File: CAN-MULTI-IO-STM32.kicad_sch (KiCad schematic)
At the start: 63 parts, among them J1 H GND L, J2 TERM, J3 USART1, J5 PWR IN, U1 STM32L433RCT3, U2 MCP2562-E-SN, U3 LMR54410, U4 ADS1015IDGS, U5 PCA9537, U6 TCA9511

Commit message: fix 2.54mm terminal block issues
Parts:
- ANA_IN1: value Conn_01x06 -> 1725698
- GPIO1: renamed from GPIO_CON1; value Conn_01x06 -> 1725698
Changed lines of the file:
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@@
 		(dnp no)
 		(fields_autoplaced yes)
-		(property "Reference" "GPIO_CON1"
+		(property "Reference" "GPIO1"
 			(at 260.35 119.38 0)
 			(effects
@@
 			)
 		)
-		(property "Value" "Conn_01x06"
+		(property "Value" "1725698"
 			(at 260.35 121.92 0)
 			(effects
@@
 					(size 1.27 1.27)
 				)
+				(hide yes)
 			)
 		)
@@
 			)
 		)
-		(property "Datasheet" "~"
+		(property "Datasheet" "https://www.mouser.com/datasheet/3/507/9/phoenix_contact_1725698_en.pdf"
 			(at 260.35 133.35 0)
 			(effects
@@
 			)
 		)
-		(property "Description" "Generic connector, single row, 01x06, script generated (kicad-library-utils/schlib/autogen/connector/)"
+		(property "Description" "Phoenix Contact 1725698"
 			(at 260.35 133.35 0)
 			(effects
@@
 			(project "CAN-MULTI-IO-STM32"
 				(path "/807782eb-8307-4922-8e5a-50da44718f8e"
-					(reference "GPIO_CON1")
+					(reference "GPIO1")
 					(unit 1)
 				)
@@
 			)
 		)
-		(property "Value" "Conn_01x06"
+		(property "Value" "1725698"
 			(at 257.81 88.8999 0)
 			(effects
@@
 				)
 				(justify left)
+				(hide yes)
 			)
 		)
@@
 			)
 		)
-		(property "Datasheet" "~"
+		(property "Datasheet" "https://www.mouser.com/datasheet/3/507/9/phoenix_contact_1725698_en.pdf"
 			(at 260.35 86.36 0)
 			(effects
@@
 			)
 		)
-		(property "Description" "Generic connector, single row, 01x06, script generated (kicad-library-utils/schlib/autogen/connector/)"
+		(property "Description" "Phoenix Contact 1725698"
 			(at 260.35 86.36 0)
 			(effects

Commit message: fix a few footprint and drc issues
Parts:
- added CVDIV1: 100n, Capacitor_SMD:C_0603_1608Metric_Pad1.08x0.95mm_HandSolder, symbol Device:C_Small
- added RVDIV1: 4K7, Resistor_SMD:R_0603_1608Metric_Pad0.98x0.95mm_HandSolder, symbol Device:R_US
- added RVDIV2: 1K0, Resistor_SMD:R_0603_1608Metric_Pad0.98x0.95mm_HandSolder, symbol Device:R_US
- U6: value TCA9511 -> PI6ULS5V9511AUEX; footprint Package_SO:VSSOP-8_3x3mm_P0.65mm -> Package_SO:MSOP-8_3x3mm_P0.65mm; Height 1.1 -> (none); Manufacturer_Name Texas Instruments -> (none); Manufacturer_Part_Number TCA9511ADGKR -> (none); Mouser Part Number 595-TCA9511ADGKR -> (none); Mouser Price/Stock https://www.mouser.co.uk/ProductDetail/Texas-Instruments/TC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 -> (none)
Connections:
- net +12V: now also RVDIV1.1
- net GND: now also CVDIV1.2, RVDIV2.2
- net STATUS: now also U1.15 (PA1); no longer U1.16 (PA2)
- new net VDIV: CVDIV1.1, RVDIV1.2, RVDIV2.1, U1.16 (PA2)
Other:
- moved on the sheet: J5

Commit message: rename gpio header
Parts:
- renumbered ANA_IN1 to ANALOG_IN1, GPIO1 to DIGITAL_IO1
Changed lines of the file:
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@@
 		(dnp no)
 		(fields_autoplaced yes)
-		(property "Reference" "GPIO1"
+		(property "Reference" "DIGITAL_IO1"
 			(at 260.35 119.38 0)
 			(effects
@@
 			(project "CAN-MULTI-IO-STM32"
 				(path "/807782eb-8307-4922-8e5a-50da44718f8e"
-					(reference "GPIO1")
+					(reference "DIGITAL_IO1")
 					(unit 1)
 				)
@@
 		(on_board yes)
 		(dnp no)
-		(property "Reference" "ANA_IN1"
+		(property "Reference" "ANALOG_IN1"
 			(at 257.81 86.3599 0)
 			(effects
@@
 			(project ""
 				(path "/807782eb-8307-4922-8e5a-50da44718f8e"
-					(reference "ANA_IN1")
+					(reference "ANALOG_IN1")
 					(unit 1)
 				)

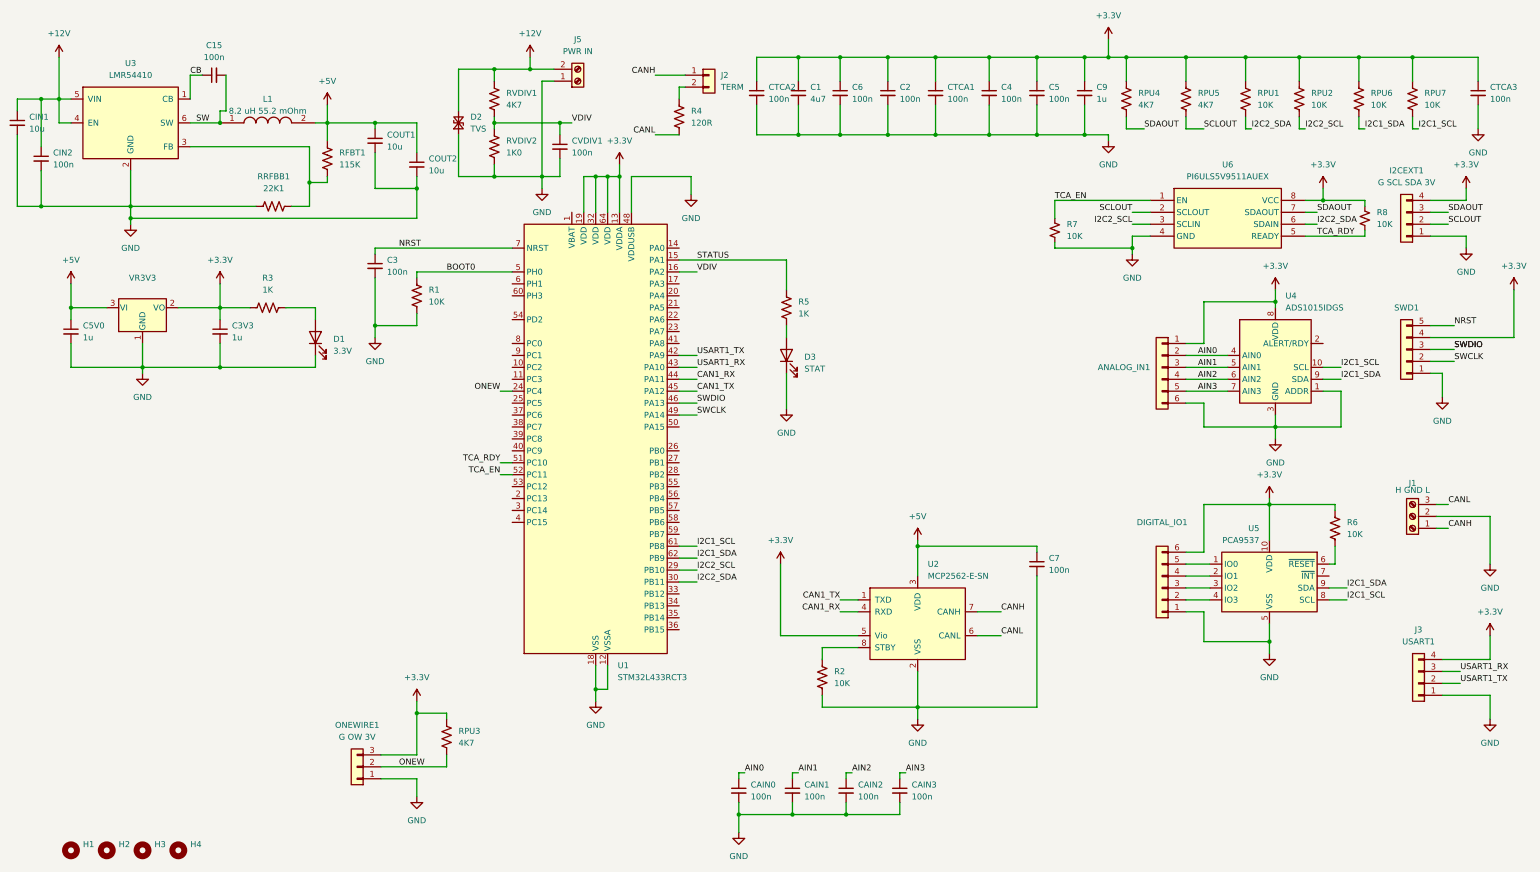
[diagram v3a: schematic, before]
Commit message: switch to STM32G0B1 micro, refactor pcb layout
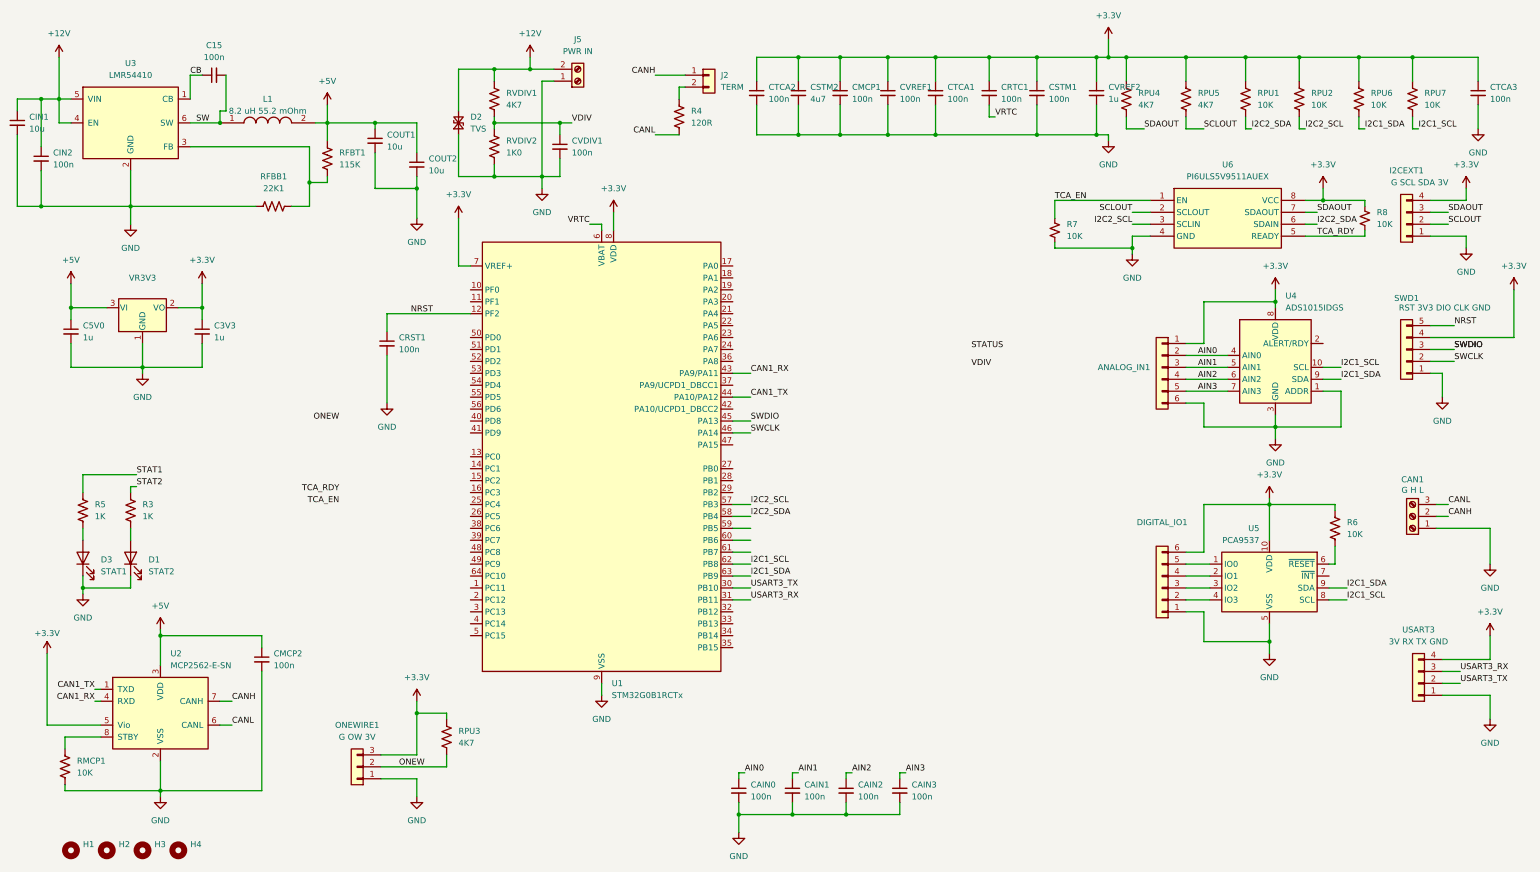
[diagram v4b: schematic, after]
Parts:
- removed R1: 10K, Resistor_SMD:R_0603_1608Metric_Pad0.98x0.95mm_HandSolder, symbol Device:R_US
- removed U1: STM32L433RCT3, Package_QFP:LQFP-64_10x10mm_P0.5mm, symbol MCU_ST_STM32L4:STM32L433RBTx
- added U1: STM32G0B1RCTx, Package_QFP:LQFP-64_10x10mm_P0.5mm, symbol MCU_ST_STM32G0:STM32G0B1RCTx
- CAN1: renamed from J1; value H GND L -> G H L; footprint TerminalBlock_Phoenix:TerminalBlock_Phoenix_MKDS-1,5-3_1x03_P5.00mm_Horizontal -> TerminalBlock_TE-Connectivity:TerminalBlock_TE_282834-3_1x03_P2.54mm_Horizontal
- D1: value 3.3V -> STAT2
- D3: value STAT -> STAT1
- SWD1: value STLINK -> RST 3V3 DIO CLK GND
- USART3: renamed from J3; value USART1 -> 3V RX TX GND
- renumbered C6 to CMCP1, C7 to CMCP2, C3 to CRST1, C4 to CRTC1, C5 to CSTM1, C1 to CSTM2, C2 to CVREF1, C9 to CVREF2, RRFBB1 to RFBB1, R2 to RMCP1
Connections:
- net +3.3V: now also U1.7 (VREF+), U1.8 (VDD); no longer R3.1
- net CAN1_RX: now also U1.43 (PA9/PA11)
- net CAN1_TX: now also U1.44 (PA10/PA12)
- net CANH: now also CAN1.2 (Pin_2); no longer CAN1.1 (Pin_1)
- net GND: now also CAN1.1 (Pin_1), U1.9 (VSS); no longer CAN1.2 (Pin_2), CRTC1.2
- net I2C1_SCL: now also U1.62 (PB8)
- net I2C1_SDA: now also U1.63 (PB9)
- net I2C2_SCL: now also U1.57 (PB3)
- net I2C2_SDA: now also U1.58 (PB4)
- net NRST: now also U1.12 (PF2)
- net STATUS: no longer R5.2
- net SWCLK: now also U1.46 (PA14)
- net SWDIO: now also U1.45 (PA13)
- net at D1.2 (A): now also R3.1; no longer R3.2
- net USART1_RX renamed USART3_RX
- net USART3_RX: now also U1.31 (PB11)
- net USART1_TX renamed USART3_TX
- net USART3_TX: now also U1.30 (PB10)
- new net STAT1: R5.2
- new net STAT2: R3.2
- new net VRTC: CRTC1.2, U1.6 (VBAT)
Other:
- moved on the sheet: C3V3, CMCP2, CRST1, CVREF2, D1, D3, R3, R5, RMCP1, U2

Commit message: final commit for tonight
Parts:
- CAN1: footprint TerminalBlock_TE-Connectivity:TerminalBlock_TE_282834-3_1x03_P2.54mm_Horizontal -> TerminalBlock_Phoenix:TerminalBlock_Phoenix_MPT-0,5-3-2.54_1x03_P2.54mm_Horizontal
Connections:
- net ONEW: now also U1.37 (PA9/UCPD1_DBCC1)
- net STAT1: now also U1.15 (PC2)
- net STAT2: now also U1.16 (PC3)
- net TCA_EN: now also U1.59 (PB5)
- net TCA_RDY: now also U1.56 (PD6)
- net VDIV: now also U1.17 (PA0)
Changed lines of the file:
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@@
+	(wire
+		(pts
+			(xy 110.49 95.25) (xy 113.03 95.25)
+		)
+		(stroke
+			(width 0)
+			(type default)
+		)
+	)
 	(wire
 		(pts
@@
 	(wire
 		(pts
+			(xy 168.91 64.77) (xy 172.72 64.77)
+		)
+		(stroke
+			(width 0)
+			(type default)
+		)
+	)
+	(wire
+		(pts
 			(xy 101.6 173.99) (xy 101.6 177.8)
 		)
@@
 	(wire
 		(pts
+			(xy 168.91 90.17) (xy 172.72 90.17)
+		)
+		(stroke
+			(width 0)
+			(type default)
+		)
+	)
+	(wire
+		(pts
 			(xy 40.64 52.07) (xy 21.59 52.07)
 		)
@@
 	(wire
 		(pts
+			(xy 110.49 113.03) (xy 113.03 113.03)
+		)
+		(stroke
+			(width 0)
+			(type default)
+		)
+	)
+	(wire
+		(pts
 			(xy 265.43 125.73) (xy 269.24 125.73)
 		)
@@
 		(pts
 			(xy 78.74 39.37) (xy 78.74 46.99)
+		)
+		(stroke
+			(width 0)
+			(type default)
+		)
+	)
+	(wire
+		(pts
+			(xy 110.49 110.49) (xy 113.03 110.49)
 		)
 		(stroke
@@
 	)
 	(label "ONEW"
-		(at 85.09 97.79 180)
-		(effects
-			(font
-				(size 1.27 1.27)
-			)
-			(justify right bottom)
+		(at 172.72 90.17 0)
+		(effects
+			(font
+				(size 1.27 1.27)
+			)
+			(justify left bottom)
 		)
 	)
@@
 		)
 	)
+	(label "STAT2"
+		(at 110.49 113.03 180)
+		(effects
+			(font
+				(size 1.27 1.27)
+			)
+			(justify right bottom)
+		)
+	)
 	(label "USART3_RX"
 		(at 172.72 135.89 0)
@@
 	)
 	(label "VDIV"
-		(at 219.71 86.36 0)
+		(at 172.72 64.77 0)
 		(effects
 			(font
@@
 	)
 	(label "TCA_RDY"
-		(at 85.09 113.03 180)
+		(at 110.49 95.25 180)
 		(effects
 			(font
@@
 		)
 	)
+	(label "STAT1"
+		(at 110.49 110.49 180)
+		(effects
+			(font
+				(size 1.27 1.27)
+			)
+			(justify right bottom)
+		)
+	)
 	(label "VRTC"
 		(at 138.43 55.88 180)
@@
 		)
 	)
-	(label "STATUS"
-		(at 219.71 82.55 0)
-		(effects
-			(font
-				(size 1.27 1.27)
-			)
-			(justify left bottom)
-		)
-	)
 	(label "I2C1_SCL"
 		(at 298.45 86.36 0)
@@
 	)
 	(label "TCA_EN"
-		(at 85.09 115.57 180)
-		(effects
-			(font
-				(size 1.27 1.27)
-			)
-			(justify right bottom)
+		(at 172.72 120.65 0)
+		(effects
+			(font
+				(size 1.27 1.27)
+			)
+			(justify left bottom)
 		)
 	)
@@
 			)
 		)
-		(property "Footprint" "TerminalBlock_TE-Connectivity:TerminalBlock_TE_282834-3_1x03_P2.54mm_Horizontal"
+		(property "Footprint" "TerminalBlock_Phoenix:TerminalBlock_Phoenix_MPT-0,5-3-2.54_1x03_P2.54mm_Horizontal"
 			(at 313.69 118.11 0)
 			(effects
